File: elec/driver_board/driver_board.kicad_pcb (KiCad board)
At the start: 2 copper layers, 200 x 108 mm, 195 parts, among them IC1 MC74HC595ADR2G-Q, IC10 MC74HC595ADR2G-Q, IC11 TPL7407LADR, IC12 TPL7407LADR, IC13 MC74HC595ADR2G-Q, IC14 TPL7407LADR, IC15 TPL7407LADR, IC16 MC74HC595ADR2G-Q, IC17 TPL7407LADR, IC18 TPL7407LADR, IC19 MC74HC595ADR2G-Q, IC2 TPL7407LADR, IC20 TPL7407LADR, IC21 TPL7407LADR, IC22 MC74HC595ADR2G-Q, IC23 TPL7407LADR, IC24 TPL7407LADR, IC25 MC74HC595ADR2G-Q, IC26 TPL7407LADR, IC27 TPL7407LADR, IC28 MC74HC595ADR2G-Q, IC29 TPL7407LADR, IC3 TPL7407LADR, IC30 TPL7407LADR, IC31 MC74HC595ADR2G-Q, IC32 TPL7407LADR, IC33 TPL7407LADR, IC34 MC74HC595ADR2G-Q, IC35 TPL7407LADR, IC36 TPL7407LADR, IC37 MC74HC595ADR2G-Q, IC38 TPL7407LADR, IC39 TPL7407LADR, IC4 MC74HC595ADR2G-Q, IC40 MC74HC595ADR2G-Q, IC41 TPL7407LADR, IC42 TPL7407LADR, IC43 MC74HC595ADR2G-Q, IC44 TPL7407LADR, IC45 TPL7407LADR, IC46 MC74HC595ADR2G-Q, IC47 TPL7407LADR, IC48 TPL7407LADR, IC49 MC74HC595ADR2G-Q, IC5 TPL7407LADR, IC50 TPL7407LADR, IC51 TPL7407LADR, IC52 MC74HC595ADR2G-Q, IC53 TPL7407LADR, IC54 TPL7407LADR, IC55 MC74HC595ADR2G-Q, IC56 TPL7407LADR, IC57 TPL7407LADR, IC58 MC74HC595ADR2G-Q, IC59 TPL7407LADR, IC6 TPL7407LADR, IC60 TPL7407LADR, IC61 MC74HC595ADR2G-Q, IC62 TPL7407LADR, IC63 TPL7407LADR, IC64 MC74HC595ADR2G-Q, IC65 TPL7407LADR, IC66 TPL7407LADR, IC67 MC74HC595ADR2G-Q, IC68 TPL7407LADR, IC69 TPL7407LADR, IC7 MC74HC595ADR2G-Q, IC70 MC74HC595ADR2G-Q, IC71 TPL7407LADR, IC72 TPL7407LADR, IC8 TPL7407LADR, IC9 TPL7407LADR, J1 MOTOR_1, J10 MOTOR_0, J11 MOTOR_1, J12 MOTOR_0, J13 MOTOR_1, J14 MOTOR_0, J15 MOTOR_1, J16 MOTOR_0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

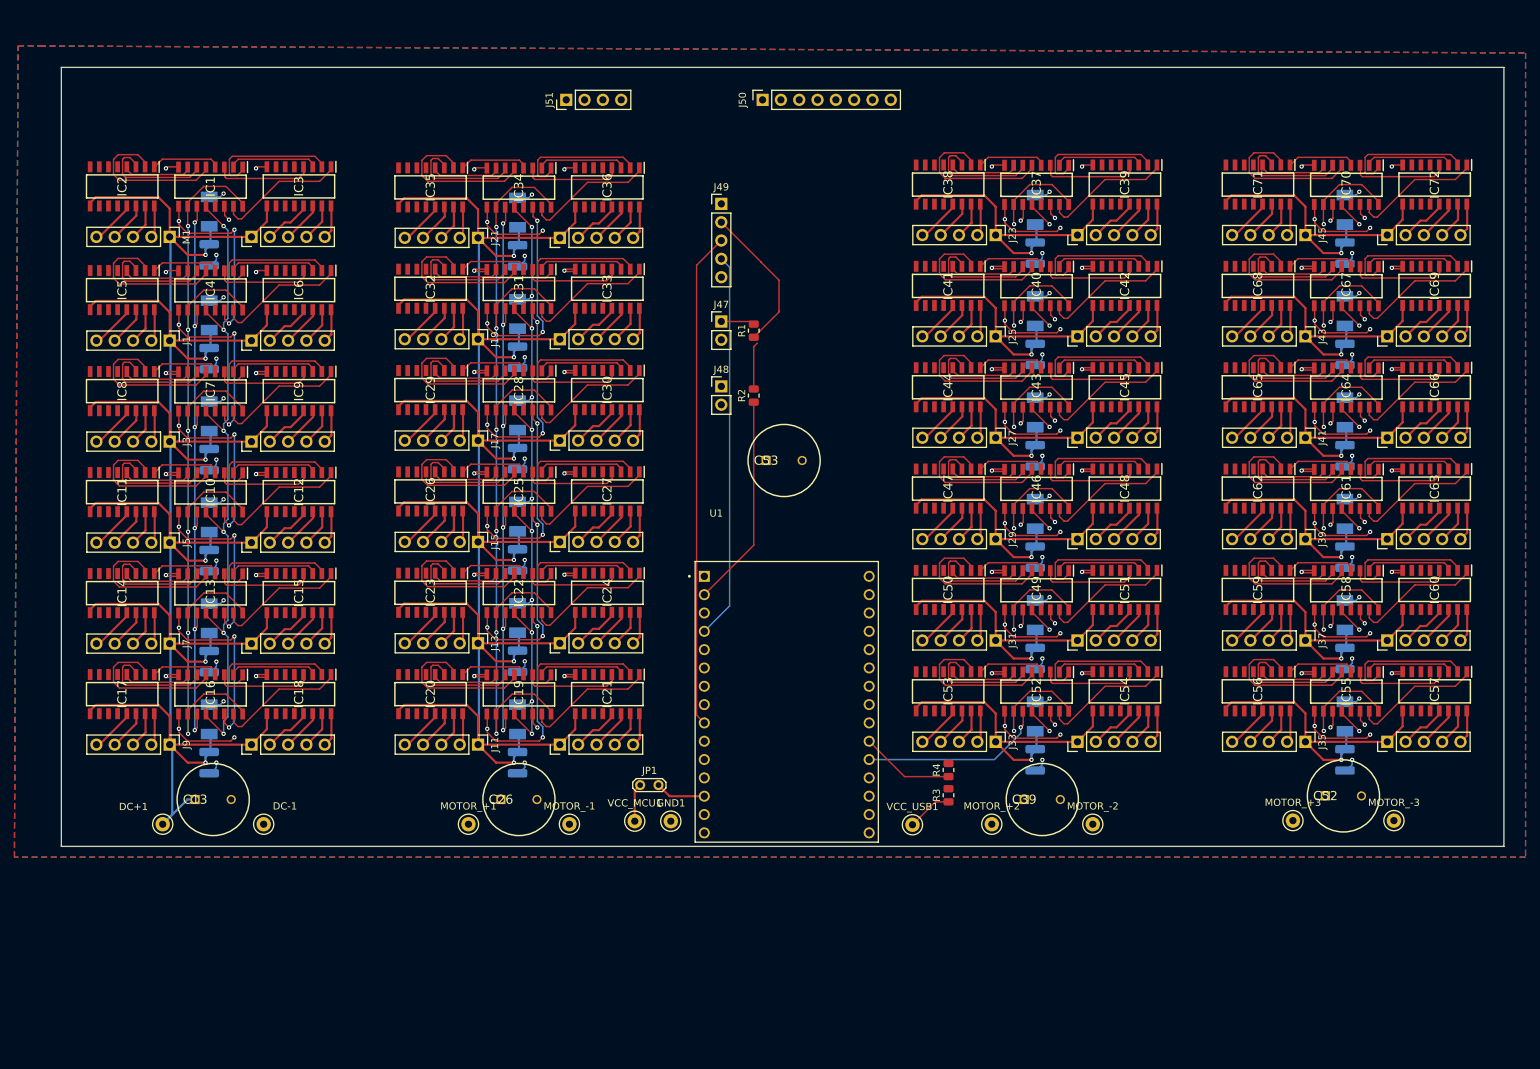
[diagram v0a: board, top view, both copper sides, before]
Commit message: [elec] New design with BKA30D-R5
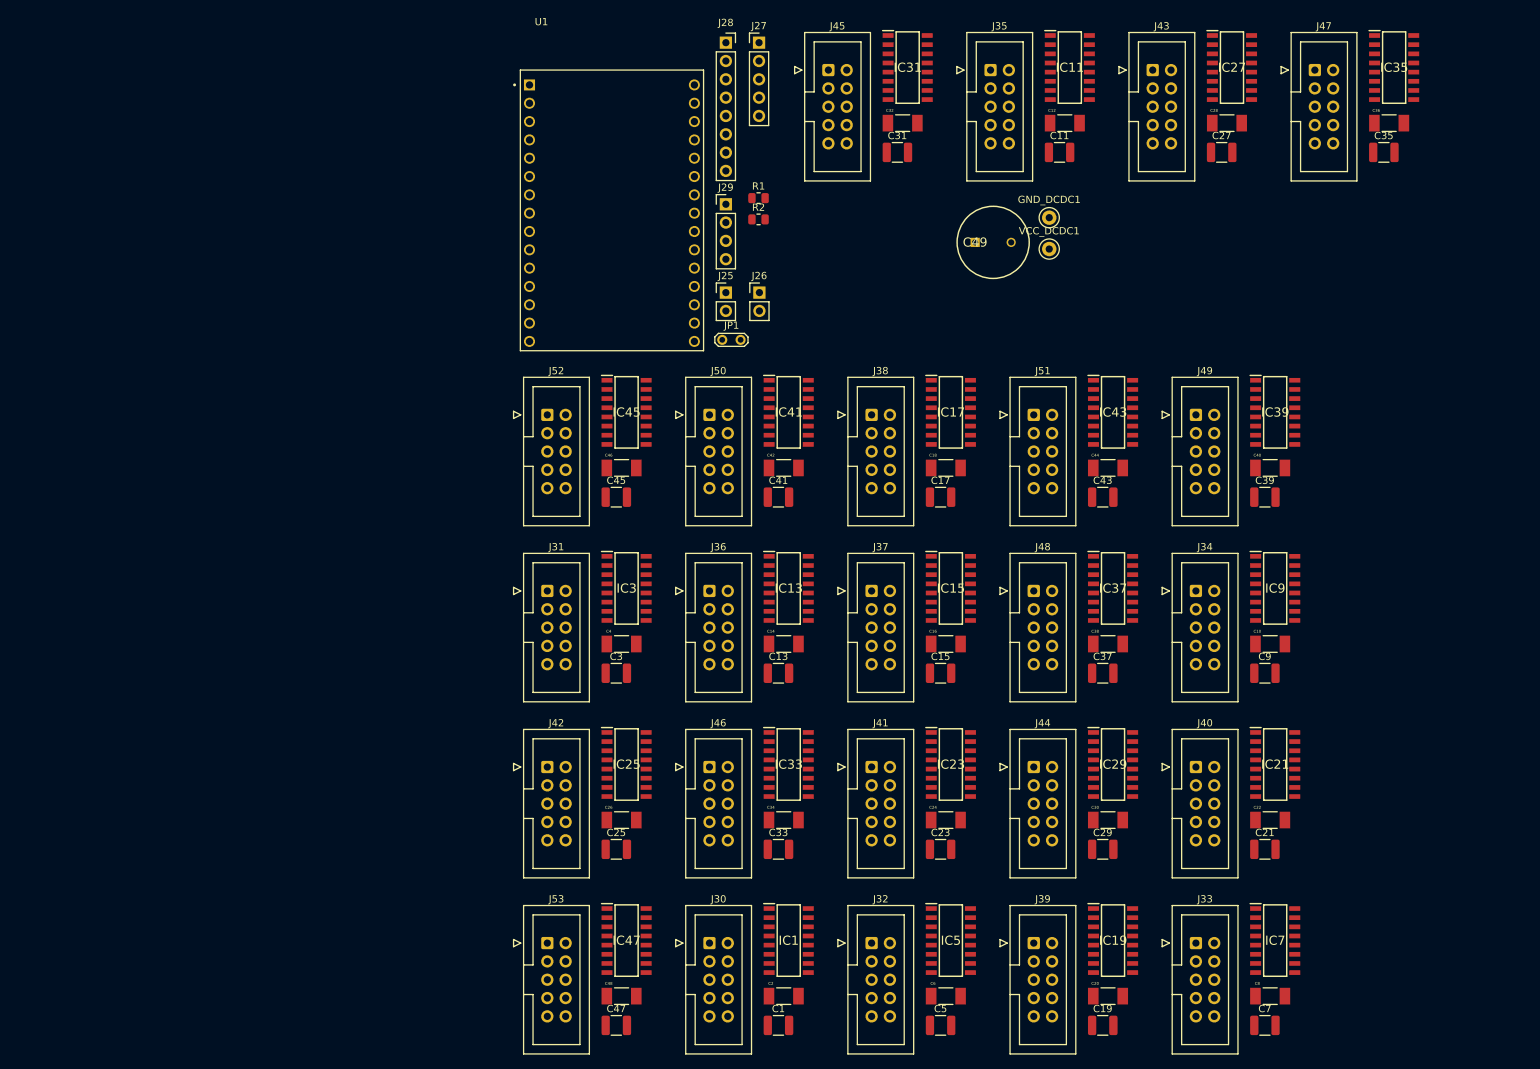
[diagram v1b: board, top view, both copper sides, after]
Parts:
- removed C50: 10µF, Capacitor_SMD:C_1210_3225Metric
- removed C51: 0.1µF, Snapeda:1808J1000392KCT_CAPC4520X200N
- removed C52, C53: ECA-1HM471, Samacsys:CAPPRD500W65D1000H2200
- removed DC+1, MOTOR_+1, MOTOR_+2, MOTOR_+3, VCC_MCU1, VCC_USB1: M+, TestPoint:TestPoint_Keystone_5000-5004_Miniature
- removed DC-1, GND1, MOTOR_-1, MOTOR_-2, MOTOR_-3: M-, TestPoint:TestPoint_Keystone_5000-5004_Miniature
- removed IC10, IC16, IC22, IC28, IC34, IC4, IC40, IC46, IC49, IC52, IC55, IC58, IC61, IC64, IC67, IC70: MC74HC595ADR2G-Q, Samacsys:SOIC127P600X175-16N
- removed IC12, IC14, IC18, IC2, IC20, IC24, IC26, IC30, IC32, IC36, IC38, IC42, IC44, IC48, IC50, IC51, IC53, IC54, IC56, IC57, IC59, IC6, IC60, IC62, IC63, IC65, IC66, IC68, IC69, IC71, IC72, IC8: TPL7407LADR, Samacsys:SOIC127P600X175-16N
- removed J1, J11, J13, J15, J17, J19, J21, J23, J3, J5, J7, J9, M1: MOTOR_1, Connector_PinHeader_2.54mm:PinHeader_1x05_P2.54mm_Vertical
- removed J10, J12, J14, J16, J18, J2, J20, J22, J24, J4, J6, J8, M2: MOTOR_0, Connector_PinHeader_2.54mm:PinHeader_1x05_P2.54mm_Vertical
- removed R3, R4: R, Resistor_SMD:R_0805_2012Metric
- added GND_DCDC1: M-, TestPoint:TestPoint_Keystone_5000-5004_Miniature, F.Cu at (166.5, 48.3)
- added J52: Conn_02x05_Counter_Clockwise, Connector_IDC:IDC-Header_2x05_P2.54mm_Vertical, F.Cu at (96.9, 75.7)
- added J53: Conn_02x05_Counter_Clockwise, Connector_IDC:IDC-Header_2x05_P2.54mm_Vertical, F.Cu at (96.9, 148.9)
- added VCC_DCDC1: M+, TestPoint:TestPoint_Keystone_5000-5004_Miniature, F.Cu at (166.5, 52.7)
- C1, C10, C11, C12, C2, C27, C28, C29, C3, C30, C31, C32, C33, C34, C35, C36, C37, C38, C4, C5, C6, C7, C8, C9: moved to F.Cu
- C13, C39: value ECA-1HM471 -> 10µF; footprint Samacsys:CAPPRD500W65D1000H2200 -> Capacitor_SMD:C_1210_3225Metric
- C14, C16, C18, C20, C22, C24, C40, C42, C44, C46, C48: value 10µF -> 0.1µF; footprint Capacitor_SMD:C_1210_3225Metric -> Snapeda:1808J1000392KCT_CAPC4520X200N; moved to F.Cu
- C15, C17, C19, C21, C23, C25, C41, C43, C45, C47: value 0.1µF -> 10µF; footprint Snapeda:1808J1000392KCT_CAPC4520X200N -> Capacitor_SMD:C_1210_3225Metric; moved to F.Cu
- C26: value ECA-1HM471 -> 0.1µF; footprint Samacsys:CAPPRD500W65D1000H2200 -> Snapeda:1808J1000392KCT_CAPC4520X200N
- C49: value 0.1µF -> ECA-1HM471; footprint Snapeda:1808J1000392KCT_CAPC4520X200N -> Samacsys:CAPPRD500W65D1000H2200; moved to F.Cu
- IC1, IC13, IC19, IC25, IC31, IC37, IC43, IC7: value MC74HC595ADR2G-Q -> TPIC6C595DG4
- IC11, IC15, IC17, IC21, IC23, IC27, IC29, IC3, IC33, IC35, IC39, IC41, IC45, IC47, IC5, IC9: value TPL7407LADR -> TPIC6C595DG4
- J25: value MOTOR_1 -> button_shutdown; footprint Connector_PinHeader_2.54mm:PinHeader_1x05_P2.54mm_Vertical -> Connector_PinHeader_2.54mm:PinHeader_1x02_P2.54mm_Vertical
- J26: value MOTOR_0 -> button_mode; footprint Connector_PinHeader_2.54mm:PinHeader_1x05_P2.54mm_Vertical -> Connector_PinHeader_2.54mm:PinHeader_1x02_P2.54mm_Vertical
- J27: value MOTOR_1 -> rotary_encoder
- J28: value MOTOR_0 -> DCF77 board; footprint Connector_PinHeader_2.54mm:PinHeader_1x05_P2.54mm_Vertical -> Connector_PinSocket_2.54mm:PinSocket_1x08_P2.54mm_Vertical
- J29: value MOTOR_1 -> RTC; footprint Connector_PinHeader_2.54mm:PinHeader_1x05_P2.54mm_Vertical -> Connector_PinHeader_2.54mm:PinHeader_1x04_P2.54mm_Vertical
- J30, J32, J34, J36, J38, J40, J42, J44, J46: value MOTOR_0 -> Conn_02x05_Counter_Clockwise; footprint Connector_PinHeader_2.54mm:PinHeader_1x05_P2.54mm_Vertical -> Connector_IDC:IDC-Header_2x05_P2.54mm_Vertical
- J31, J33, J35, J37, J39, J41, J43, J45: value MOTOR_1 -> Conn_02x05_Counter_Clockwise; footprint Connector_PinHeader_2.54mm:PinHeader_1x05_P2.54mm_Vertical -> Connector_IDC:IDC-Header_2x05_P2.54mm_Vertical
- J47: value button_shutdown -> Conn_02x05_Counter_Clockwise; footprint Connector_PinHeader_2.54mm:PinHeader_1x02_P2.54mm_Vertical -> Connector_IDC:IDC-Header_2x05_P2.54mm_Vertical
- J48: value button_mode -> Conn_02x05_Counter_Clockwise; footprint Connector_PinHeader_2.54mm:PinHeader_1x02_P2.54mm_Vertical -> Connector_IDC:IDC-Header_2x05_P2.54mm_Vertical
- J49: value rotary_encoder -> Conn_02x05_Counter_Clockwise; footprint Connector_PinHeader_2.54mm:PinHeader_1x05_P2.54mm_Vertical -> Connector_IDC:IDC-Header_2x05_P2.54mm_Vertical
- J50: value DCF77 board -> Conn_02x05_Counter_Clockwise; footprint Connector_PinSocket_2.54mm:PinSocket_1x08_P2.54mm_Vertical -> Connector_IDC:IDC-Header_2x05_P2.54mm_Vertical
- J51: value RTC -> Conn_02x05_Counter_Clockwise; footprint Connector_PinHeader_2.54mm:PinHeader_1x04_P2.54mm_Vertical -> Connector_IDC:IDC-Header_2x05_P2.54mm_Vertical
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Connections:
- C1 pad 1: /motor_driver0/VCC_MOTOR -> VCC
- C10 pad 1: /motor_driver0/VCC_MOTOR -> VCC
- C11 pad 1: /motor_driver0/VCC_MOTOR -> VCC
- C12 pad 1: /motor_driver0/VCC_MOTOR -> VCC
- C13 pad 1: /motor_driver0/VCC_MOTOR -> VCC
- C14 pad 1: /motor_driver10/VCC_MOTOR -> VCC
- C15 pad 1: /motor_driver10/VCC_MOTOR -> VCC
- C16 pad 1: /motor_driver10/VCC_MOTOR -> VCC
- C17 pad 1: /motor_driver10/VCC_MOTOR -> VCC
- C18 pad 1: /motor_driver10/VCC_MOTOR -> VCC
- C19 pad 1: /motor_driver10/VCC_MOTOR -> VCC
- C2 pad 1: /motor_driver0/VCC_MOTOR -> VCC
- C20 pad 1: /motor_driver10/VCC_MOTOR -> VCC
- C21 pad 1: /motor_driver10/VCC_MOTOR -> VCC
- C22 pad 1: /motor_driver10/VCC_MOTOR -> VCC
- C23 pad 1: /motor_driver10/VCC_MOTOR -> VCC
- C24 pad 1: /motor_driver10/VCC_MOTOR -> VCC
- C25 pad 1: /motor_driver10/VCC_MOTOR -> VCC
- C26 pad 1: /motor_driver10/VCC_MOTOR -> VCC
- C27 pad 1: /motor_driver12/VCC_MOTOR -> VCC
- C28 pad 1: /motor_driver12/VCC_MOTOR -> VCC
- C29 pad 1: /motor_driver12/VCC_MOTOR -> VCC
- C3 pad 1: /motor_driver0/VCC_MOTOR -> VCC
- C30 pad 1: /motor_driver12/VCC_MOTOR -> VCC
- C31 pad 1: /motor_driver12/VCC_MOTOR -> VCC
- C32 pad 1: /motor_driver12/VCC_MOTOR -> VCC
- C33 pad 1: /motor_driver12/VCC_MOTOR -> VCC
- C34 pad 1: /motor_driver12/VCC_MOTOR -> VCC
- C35 pad 1: /motor_driver12/VCC_MOTOR -> VCC
- C36 pad 1: /motor_driver12/VCC_MOTOR -> VCC
- C37 pad 1: /motor_driver12/VCC_MOTOR -> VCC
- C38 pad 1: /motor_driver12/VCC_MOTOR -> VCC
- C39 pad 1: /motor_driver12/VCC_MOTOR -> VCC
- C4 pad 1: /motor_driver0/VCC_MOTOR -> VCC
- C40 pad 1: /motor_driver18/VCC_MOTOR -> VCC
- C41 pad 1: /motor_driver18/VCC_MOTOR -> VCC
- C42 pad 1: /motor_driver18/VCC_MOTOR -> VCC
- C43 pad 1: /motor_driver18/VCC_MOTOR -> VCC
- C44 pad 1: /motor_driver18/VCC_MOTOR -> VCC
- C45 pad 1: /motor_driver18/VCC_MOTOR -> VCC
- C46 pad 1: /motor_driver18/VCC_MOTOR -> VCC
- C47 pad 1: /motor_driver18/VCC_MOTOR -> VCC
- C48 pad 1: /motor_driver18/VCC_MOTOR -> VCC
- C49 pad 1: /motor_driver18/VCC_MOTOR -> VCC
- C5 pad 1: /motor_driver0/VCC_MOTOR -> VCC
- C6 pad 1: /motor_driver0/VCC_MOTOR -> VCC
- C7 pad 1: /motor_driver0/VCC_MOTOR -> VCC
- C8 pad 1: /motor_driver0/VCC_MOTOR -> VCC
- C9 pad 1: /motor_driver0/VCC_MOTOR -> VCC
- IC1 pad 1: Net-(IC1-QB) -> VCC
- IC1 pad 10: VCC_CMD -> SHIFT_CLOCK
- IC1 pad 11: SHIFT_CLOCK -> /motor_driver0/M1_23
- IC1 pad 12: LATCH_CLOCK -> /motor_driver0/M1_4
- IC1 pad 13: GND -> /motor_driver0/VCC_HALL
- IC1 pad 14: /control_board/DATA_OUT -> unconnected-(IC1-DRAIN7-Pad14)
- IC1 pad 15: Net-(IC1-QA) -> LATCH_CLOCK
- IC1 pad 16: VCC_CMD -> GND
- IC1 pad 2: Net-(IC1-QC) -> /control_board/DATA_OUT
- IC1 pad 3: Net-(IC1-QD) -> /motor_driver0/M0_1
- IC1 pad 4: Net-(IC1-QE) -> /motor_driver0/M0_23
- IC1 pad 5: Net-(IC1-QF) -> /motor_driver0/M0_4
- IC1 pad 6: Net-(IC1-QG) -> /motor_driver0/M1_1
- IC1 pad 7: Net-(IC1-QH) -> VCC
- IC11 pad 1: Net-(IC10-QE) -> VCC
- IC11 pad 10: unconnected-(IC11-OUT7-Pad10) -> SHIFT_CLOCK
- IC11 pad 11: unconnected-(IC11-OUT6-Pad11) -> /motor_driver5/M1_23
- IC11 pad 12: unconnected-(IC11-OUT5-Pad12) -> /motor_driver5/M1_4
- IC11 pad 13: Net-(IC11-OUT4) -> /motor_driver5/VCC_HALL
- IC11 pad 14: Net-(IC11-OUT3) -> unconnected-(IC11-DRAIN7-Pad14)
- IC11 pad 15: Net-(IC11-OUT2) -> LATCH_CLOCK
- IC11 pad 16: Net-(IC11-OUT1) -> GND
- IC11 pad 2: Net-(IC10-QF) -> /motor_driver4/DATA_OUT
- IC11 pad 3: Net-(IC10-QG) -> /motor_driver5/M0_1
- IC11 pad 4: Net-(IC10-QH) -> /motor_driver5/M0_23
- IC11 pad 5: unconnected-(IC11-IN5-Pad5) -> /motor_driver5/M0_4
- IC11 pad 6: unconnected-(IC11-IN6-Pad6) -> /motor_driver5/M1_1
- IC11 pad 7: unconnected-(IC11-IN7-Pad7) -> VCC
- IC11 pad 9: /motor_driver0/VCC_MOTOR -> /motor_driver5/DATA_OUT
- IC13 pad 1: Net-(IC13-QB) -> VCC
- IC13 pad 10: VCC_CMD -> SHIFT_CLOCK
- IC13 pad 11: SHIFT_CLOCK -> /motor_driver6/M1_23
- IC13 pad 12: LATCH_CLOCK -> /motor_driver6/M1_4
- IC13 pad 13: GND -> /motor_driver6/VCC_HALL
- IC13 pad 14: /motor_driver3/DATA_OUT -> unconnected-(IC13-DRAIN7-Pad14)
- IC13 pad 15: Net-(IC13-QA) -> LATCH_CLOCK
- IC13 pad 16: VCC_CMD -> GND
- IC13 pad 2: Net-(IC13-QC) -> /motor_driver5/DATA_OUT
- IC13 pad 3: Net-(IC13-QD) -> /motor_driver6/M0_1
- IC13 pad 4: Net-(IC13-QE) -> /motor_driver6/M0_23
- IC13 pad 5: Net-(IC13-QF) -> /motor_driver6/M0_4
- IC13 pad 6: Net-(IC13-QG) -> /motor_driver6/M1_1
- IC13 pad 7: Net-(IC13-QH) -> VCC
- IC13 pad 9: /motor_driver4/DATA_OUT -> /motor_driver6/DATA_OUT
- IC15 pad 1: Net-(IC13-QA) -> VCC
- IC15 pad 10: unconnected-(IC15-OUT7-Pad10) -> SHIFT_CLOCK
- IC15 pad 11: unconnected-(IC15-OUT6-Pad11) -> /motor_driver7/M1_23
- IC15 pad 12: unconnected-(IC15-OUT5-Pad12) -> /motor_driver7/M1_4
- IC15 pad 13: Net-(IC15-OUT4) -> /motor_driver7/VCC_HALL
- IC15 pad 14: Net-(IC15-OUT3) -> unconnected-(IC15-DRAIN7-Pad14)
- IC15 pad 15: Net-(IC15-OUT2) -> LATCH_CLOCK
- IC15 pad 16: Net-(IC15-OUT1) -> GND
- IC15 pad 2: Net-(IC13-QB) -> /motor_driver6/DATA_OUT
- IC15 pad 3: Net-(IC13-QC) -> /motor_driver7/M0_1
- IC15 pad 4: Net-(IC13-QD) -> /motor_driver7/M0_23
- IC15 pad 5: unconnected-(IC15-IN5-Pad5) -> /motor_driver7/M0_4
- IC15 pad 6: unconnected-(IC15-IN6-Pad6) -> /motor_driver7/M1_1
- IC15 pad 7: unconnected-(IC15-IN7-Pad7) -> VCC
- IC15 pad 9: /motor_driver0/VCC_MOTOR -> /motor_driver7/DATA_OUT
- IC17 pad 1: Net-(IC16-QE) -> VCC
- IC17 pad 10: unconnected-(IC17-OUT7-Pad10) -> SHIFT_CLOCK
- IC17 pad 11: unconnected-(IC17-OUT6-Pad11) -> /motor_driver8/M1_23
- IC17 pad 12: unconnected-(IC17-OUT5-Pad12) -> /motor_driver8/M1_4
- IC17 pad 13: Net-(IC17-OUT4) -> /motor_driver8/VCC_HALL
- IC17 pad 14: Net-(IC17-OUT3) -> unconnected-(IC17-DRAIN7-Pad14)
- IC17 pad 15: Net-(IC17-OUT2) -> LATCH_CLOCK
- IC17 pad 16: Net-(IC17-OUT1) -> GND
- IC17 pad 2: Net-(IC16-QF) -> /motor_driver7/DATA_OUT
- IC17 pad 3: Net-(IC16-QG) -> /motor_driver8/M0_1
- IC17 pad 4: Net-(IC16-QH) -> /motor_driver8/M0_23
- IC17 pad 5: unconnected-(IC17-IN5-Pad5) -> /motor_driver8/M0_4
- IC17 pad 6: unconnected-(IC17-IN6-Pad6) -> /motor_driver8/M1_1
- IC17 pad 7: unconnected-(IC17-IN7-Pad7) -> VCC
- IC17 pad 9: /motor_driver0/VCC_MOTOR -> /motor_driver8/DATA_OUT
- IC19 pad 1: Net-(IC19-QB) -> VCC
- IC19 pad 10: VCC_CMD -> SHIFT_CLOCK
- IC19 pad 11: SHIFT_CLOCK -> /motor_driver9/M1_23
- IC19 pad 12: LATCH_CLOCK -> /motor_driver9/M1_4
- IC19 pad 13: GND -> /motor_driver9/VCC_HALL
- IC19 pad 14: /motor_driver5/DATA_OUT -> unconnected-(IC19-DRAIN7-Pad14)
- IC19 pad 15: Net-(IC19-QA) -> LATCH_CLOCK
- IC19 pad 16: VCC_CMD -> GND
- IC19 pad 2: Net-(IC19-QC) -> /motor_driver8/DATA_OUT
- IC19 pad 3: Net-(IC19-QD) -> /motor_driver9/M0_1
- IC19 pad 4: Net-(IC19-QE) -> /motor_driver9/M0_23
- IC19 pad 5: Net-(IC19-QF) -> /motor_driver9/M0_4
- IC19 pad 6: Net-(IC19-QG) -> /motor_driver9/M1_1
- IC19 pad 7: Net-(IC19-QH) -> VCC
- IC19 pad 9: /motor_driver6/DATA_OUT -> /motor_driver10/DATA_IN
- IC21 pad 1: Net-(IC19-QA) -> VCC
- IC21 pad 10: unconnected-(IC21-OUT7-Pad10) -> SHIFT_CLOCK
- IC21 pad 11: unconnected-(IC21-OUT6-Pad11) -> /motor_driver10/M1_23
- IC21 pad 12: unconnected-(IC21-OUT5-Pad12) -> /motor_driver10/M1_4
- IC21 pad 13: Net-(IC21-OUT4) -> /motor_driver10/VCC_HALL
- IC21 pad 14: Net-(IC21-OUT3) -> unconnected-(IC21-DRAIN7-Pad14)
- IC21 pad 15: Net-(IC21-OUT2) -> LATCH_CLOCK
- IC21 pad 16: Net-(IC21-OUT1) -> GND
- IC21 pad 2: Net-(IC19-QB) -> /motor_driver10/DATA_IN
- IC21 pad 3: Net-(IC19-QC) -> /motor_driver10/M0_1
- IC21 pad 4: Net-(IC19-QD) -> /motor_driver10/M0_23
- IC21 pad 5: unconnected-(IC21-IN5-Pad5) -> /motor_driver10/M0_4
- IC21 pad 6: unconnected-(IC21-IN6-Pad6) -> /motor_driver10/M1_1
- IC21 pad 7: unconnected-(IC21-IN7-Pad7) -> VCC
- IC21 pad 9: /motor_driver10/VCC_MOTOR -> /motor_driver10/DATA_OUT
- IC23 pad 1: Net-(IC22-QE) -> VCC
- IC23 pad 10: unconnected-(IC23-OUT7-Pad10) -> SHIFT_CLOCK
- IC23 pad 11: unconnected-(IC23-OUT6-Pad11) -> /motor_driver11/M1_23
- IC23 pad 12: unconnected-(IC23-OUT5-Pad12) -> /motor_driver11/M1_4
- IC23 pad 13: Net-(IC23-OUT4) -> /motor_driver11/VCC_HALL
- IC23 pad 14: Net-(IC23-OUT3) -> unconnected-(IC23-DRAIN7-Pad14)
- IC23 pad 15: Net-(IC23-OUT2) -> LATCH_CLOCK
- IC23 pad 16: Net-(IC23-OUT1) -> GND
- IC23 pad 2: Net-(IC22-QF) -> /motor_driver10/DATA_OUT
- IC23 pad 3: Net-(IC22-QG) -> /motor_driver11/M0_1
- IC23 pad 4: Net-(IC22-QH) -> /motor_driver11/M0_23
- IC23 pad 5: unconnected-(IC23-IN5-Pad5) -> /motor_driver11/M0_4
- IC23 pad 6: unconnected-(IC23-IN6-Pad6) -> /motor_driver11/M1_1
- IC23 pad 7: unconnected-(IC23-IN7-Pad7) -> VCC
- IC23 pad 9: /motor_driver10/VCC_MOTOR -> /motor_driver11/DATA_OUT
- IC25 pad 1: Net-(IC25-QB) -> VCC
- IC25 pad 10: VCC_CMD -> SHIFT_CLOCK
- IC25 pad 11: SHIFT_CLOCK -> /motor_driver12/M1_23
- IC25 pad 12: LATCH_CLOCK -> /motor_driver12/M1_4
- IC25 pad 13: GND -> /motor_driver12/VCC_HALL
- IC25 pad 14: /motor_driver7/DATA_OUT -> unconnected-(IC25-DRAIN7-Pad14)
- IC25 pad 15: Net-(IC25-QA) -> LATCH_CLOCK
- IC25 pad 16: VCC_CMD -> GND
- IC25 pad 2: Net-(IC25-QC) -> /motor_driver11/DATA_OUT
- IC25 pad 3: Net-(IC25-QD) -> /motor_driver12/M0_1
- IC25 pad 4: Net-(IC25-QE) -> /motor_driver12/M0_23
- IC25 pad 5: Net-(IC25-QF) -> /motor_driver12/M0_4
- IC25 pad 6: Net-(IC25-QG) -> /motor_driver12/M1_1
- IC25 pad 7: Net-(IC25-QH) -> VCC
- IC25 pad 9: /motor_driver8/DATA_OUT -> /motor_driver12/DATA_OUT
- IC27 pad 1: Net-(IC25-QA) -> VCC
- IC27 pad 10: unconnected-(IC27-OUT7-Pad10) -> SHIFT_CLOCK
- IC27 pad 11: unconnected-(IC27-OUT6-Pad11) -> /motor_driver13/M1_23
- IC27 pad 12: unconnected-(IC27-OUT5-Pad12) -> /motor_driver13/M1_4
- IC27 pad 13: Net-(IC27-OUT4) -> /motor_driver13/VCC_HALL
- IC27 pad 14: Net-(IC27-OUT3) -> unconnected-(IC27-DRAIN7-Pad14)
- IC27 pad 15: Net-(IC27-OUT2) -> LATCH_CLOCK
- IC27 pad 16: Net-(IC27-OUT1) -> GND
- IC27 pad 2: Net-(IC25-QB) -> /motor_driver12/DATA_OUT
- IC27 pad 3: Net-(IC25-QC) -> /motor_driver13/M0_1
- IC27 pad 4: Net-(IC25-QD) -> /motor_driver13/M0_23
- IC27 pad 5: unconnected-(IC27-IN5-Pad5) -> /motor_driver13/M0_4
- IC27 pad 6: unconnected-(IC27-IN6-Pad6) -> /motor_driver13/M1_1
- IC27 pad 7: unconnected-(IC27-IN7-Pad7) -> VCC
- IC27 pad 9: /motor_driver10/VCC_MOTOR -> /motor_driver13/DATA_OUT
- IC29 pad 1: Net-(IC28-QE) -> VCC
- IC29 pad 10: unconnected-(IC29-OUT7-Pad10) -> SHIFT_CLOCK
- IC29 pad 11: unconnected-(IC29-OUT6-Pad11) -> /motor_driver14/M1_23
- IC29 pad 12: unconnected-(IC29-OUT5-Pad12) -> /motor_driver14/M1_4
- IC29 pad 13: Net-(IC29-OUT4) -> /motor_driver14/VCC_HALL
- IC29 pad 14: Net-(IC29-OUT3) -> unconnected-(IC29-DRAIN7-Pad14)
- IC29 pad 15: Net-(IC29-OUT2) -> LATCH_CLOCK
- IC29 pad 16: Net-(IC29-OUT1) -> GND
- IC29 pad 2: Net-(IC28-QF) -> /motor_driver13/DATA_OUT
- IC29 pad 3: Net-(IC28-QG) -> /motor_driver14/M0_1
- IC29 pad 4: Net-(IC28-QH) -> /motor_driver14/M0_23
- IC29 pad 5: unconnected-(IC29-IN5-Pad5) -> /motor_driver14/M0_4
- IC29 pad 6: unconnected-(IC29-IN6-Pad6) -> /motor_driver14/M1_1
- IC29 pad 7: unconnected-(IC29-IN7-Pad7) -> VCC
- IC29 pad 9: /motor_driver10/VCC_MOTOR -> /motor_driver14/DATA_OUT
- IC3 pad 1: Net-(IC1-QA) -> VCC
- IC3 pad 10: unconnected-(IC3-OUT7-Pad10) -> SHIFT_CLOCK
- IC3 pad 11: unconnected-(IC3-OUT6-Pad11) -> /motor_driver1/M1_23
- IC3 pad 12: unconnected-(IC3-OUT5-Pad12) -> /motor_driver1/M1_4
- IC3 pad 13: Net-(IC3-OUT4) -> /motor_driver1/VCC_HALL
- IC3 pad 14: Net-(IC3-OUT3) -> unconnected-(IC3-DRAIN7-Pad14)
- IC3 pad 15: Net-(IC3-OUT2) -> LATCH_CLOCK
- IC3 pad 16: Net-(IC3-OUT1) -> GND
- IC3 pad 2: Net-(IC1-QB) -> /motor_driver0/DATA_OUT
- IC3 pad 3: Net-(IC1-QC) -> /motor_driver1/M0_1
- IC3 pad 4: Net-(IC1-QD) -> /motor_driver1/M0_23
- IC3 pad 5: unconnected-(IC3-IN5-Pad5) -> /motor_driver1/M0_4
- IC3 pad 6: unconnected-(IC3-IN6-Pad6) -> /motor_driver1/M1_1
- IC3 pad 7: unconnected-(IC3-IN7-Pad7) -> VCC
- IC3 pad 9: /motor_driver0/VCC_MOTOR -> /motor_driver1/DATA_OUT
- IC31 pad 1: Net-(IC31-QB) -> VCC
- IC31 pad 10: VCC_CMD -> SHIFT_CLOCK
- IC31 pad 11: SHIFT_CLOCK -> /motor_driver15/M1_23
- IC31 pad 12: LATCH_CLOCK -> /motor_driver15/M1_4
- IC31 pad 13: GND -> /motor_driver15/VCC_HALL
- IC31 pad 14: /motor_driver10/DATA_IN -> unconnected-(IC31-DRAIN7-Pad14)
- IC31 pad 15: Net-(IC31-QA) -> LATCH_CLOCK
- IC31 pad 16: VCC_CMD -> GND
- IC31 pad 2: Net-(IC31-QC) -> /motor_driver14/DATA_OUT
- IC31 pad 3: Net-(IC31-QD) -> /motor_driver15/M0_1
- IC31 pad 4: Net-(IC31-QE) -> /motor_driver15/M0_23
- IC31 pad 5: Net-(IC31-QF) -> /motor_driver15/M0_4
- IC31 pad 6: Net-(IC31-QG) -> /motor_driver15/M1_1
- IC31 pad 7: Net-(IC31-QH) -> VCC
- IC31 pad 9: /motor_driver10/DATA_OUT -> /motor_driver15/DATA_OUT
- IC33 pad 1: Net-(IC31-QA) -> VCC
- IC33 pad 10: unconnected-(IC33-OUT7-Pad10) -> SHIFT_CLOCK
- IC33 pad 11: unconnected-(IC33-OUT6-Pad11) -> /motor_driver16/M1_23
- IC33 pad 12: unconnected-(IC33-OUT5-Pad12) -> /motor_driver16/M1_4
- IC33 pad 13: Net-(IC33-OUT4) -> /motor_driver16/VCC_HALL
- IC33 pad 14: Net-(IC33-OUT3) -> unconnected-(IC33-DRAIN7-Pad14)
- IC33 pad 15: Net-(IC33-OUT2) -> LATCH_CLOCK
- IC33 pad 16: Net-(IC33-OUT1) -> GND
- IC33 pad 2: Net-(IC31-QB) -> /motor_driver15/DATA_OUT
- IC33 pad 3: Net-(IC31-QC) -> /motor_driver16/M0_1
- IC33 pad 4: Net-(IC31-QD) -> /motor_driver16/M0_23
- IC33 pad 5: unconnected-(IC33-IN5-Pad5) -> /motor_driver16/M0_4
- IC33 pad 6: unconnected-(IC33-IN6-Pad6) -> /motor_driver16/M1_1
- IC33 pad 7: unconnected-(IC33-IN7-Pad7) -> VCC
- IC33 pad 9: /motor_driver10/VCC_MOTOR -> /motor_driver16/DATA_OUT
- IC35 pad 1: Net-(IC34-QE) -> VCC
- IC35 pad 10: unconnected-(IC35-OUT7-Pad10) -> SHIFT_CLOCK
- IC35 pad 11: unconnected-(IC35-OUT6-Pad11) -> /motor_driver17/M1_23
- IC35 pad 12: unconnected-(IC35-OUT5-Pad12) -> /motor_driver17/M1_4
- IC35 pad 13: Net-(IC35-OUT4) -> /motor_driver17/VCC_HALL
- IC35 pad 14: Net-(IC35-OUT3) -> unconnected-(IC35-DRAIN7-Pad14)
- IC35 pad 15: Net-(IC35-OUT2) -> LATCH_CLOCK
- IC35 pad 16: Net-(IC35-OUT1) -> GND
- IC35 pad 2: Net-(IC34-QF) -> /motor_driver16/DATA_OUT
- IC35 pad 3: Net-(IC34-QG) -> /motor_driver17/M0_1
- IC35 pad 4: Net-(IC34-QH) -> /motor_driver17/M0_23
- IC35 pad 5: unconnected-(IC35-IN5-Pad5) -> /motor_driver17/M0_4
- IC35 pad 6: unconnected-(IC35-IN6-Pad6) -> /motor_driver17/M1_1
- IC35 pad 7: unconnected-(IC35-IN7-Pad7) -> VCC
- IC35 pad 9: /motor_driver10/VCC_MOTOR -> /motor_driver17/DATA_OUT
- IC37 pad 1: Net-(IC37-QB) -> VCC
- IC37 pad 10: VCC_CMD -> SHIFT_CLOCK
- IC37 pad 11: SHIFT_CLOCK -> /motor_driver18/M1_23
- IC37 pad 12: LATCH_CLOCK -> /motor_driver18/M1_4
- IC37 pad 13: GND -> /motor_driver18/VCC_HALL
- IC37 pad 14: /motor_driver11/DATA_OUT -> unconnected-(IC37-DRAIN7-Pad14)
- IC37 pad 15: Net-(IC37-QA) -> LATCH_CLOCK
- IC37 pad 16: VCC_CMD -> GND
- IC37 pad 2: Net-(IC37-QC) -> /motor_driver17/DATA_OUT
- IC37 pad 3: Net-(IC37-QD) -> /motor_driver18/M0_1
- IC37 pad 4: Net-(IC37-QE) -> /motor_driver18/M0_23
- IC37 pad 5: Net-(IC37-QF) -> /motor_driver18/M0_4
- IC37 pad 6: Net-(IC37-QG) -> /motor_driver18/M1_1
- IC37 pad 7: Net-(IC37-QH) -> VCC
- IC37 pad 9: /motor_driver12/DATA_OUT -> /motor_driver18/DATA_OUT
- IC39 pad 1: Net-(IC37-QA) -> VCC
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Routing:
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- removed copper zone on B.Cu, net GND
- removed copper zone on F.Cu, net GND
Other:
- board outline removed

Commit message: [elec] continue routing
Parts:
- removed IC25, IC27, IC29, IC31, IC33, IC35, IC37, IC39, IC41, IC43, IC45, IC47: TPIC6C595DG4, Samacsys:SOIC127P600X175-16N
- removed J30, J31, J32, J33, J34, J35, J36, J37, J38, J39, J40, J41, J42, J43, J44, J45, J46, J47, J48, J49, J50, J51, J52, J53: Conn_02x05_Counter_Clockwise, Connector_IDC:IDC-Header_2x05_P2.54mm_Vertical
- added Cl1: 4.2nF, Capacitor_SMD:C_1206_3216Metric, F.Cu at (48.1, 32.6)
- added IC10: TPIC6C595DG4, Samacsys:SOIC127P600X175-16N, F.Cu at (164.5, 54.0)
- added IC12: TPIC6C595DG4, Samacsys:SOIC127P600X175-16N, F.Cu at (164.5, 25.9)
- added IC14: TPIC6C595DG4, Samacsys:SOIC127P600X175-16N, F.Cu at (189.2, 39.9)
- added IC16: TPIC6C595DG4, Samacsys:SOIC127P600X175-16N, F.Cu at (213.9, 54.0)
- added IC18: TPIC6C595DG4, Samacsys:SOIC127P600X175-16N, F.Cu at (213.9, 25.9)
- added IC2: TPIC6C595DG4, Samacsys:SOIC127P600X175-16N, F.Cu at (90.5, 39.9)
- added IC20: TPIC6C595DG4, Samacsys:SOIC127P600X175-16N, F.Cu at (238.6, 39.9)
- added IC22: TPIC6C595DG4, Samacsys:SOIC127P600X175-16N, F.Cu at (263.3, 54.0)
- added IC24: TPIC6C595DG4, Samacsys:SOIC127P600X175-16N, F.Cu at (263.3, 25.9)
- added IC4: TPIC6C595DG4, Samacsys:SOIC127P600X175-16N, F.Cu at (115.1, 54.0)
- added IC6: TPIC6C595DG4, Samacsys:SOIC127P600X175-16N, F.Cu at (115.1, 25.9)
- added IC8: TPIC6C595DG4, Samacsys:SOIC127P600X175-16N, F.Cu at (139.8, 39.9)
- added J1: Connector to the motor board, Connector_JST:JST_PH_B10B-PH-K_1x10_P2.00mm_Vertical, F.Cu at (87.4, 18.3)
- added J10: Connector to the motor board, Connector_JST:JST_PH_B10B-PH-K_1x10_P2.00mm_Vertical, F.Cu at (161.5, 46.4)
- added J11: Connector to the motor board, Connector_JST:JST_PH_B10B-PH-K_1x10_P2.00mm_Vertical, F.Cu at (161.5, 32.3)
- added J12: Connector to the motor board, Connector_JST:JST_PH_B10B-PH-K_1x10_P2.00mm_Vertical, F.Cu at (161.5, 18.3)
- added J13: Connector to the motor board, Connector_JST:JST_PH_B10B-PH-K_1x10_P2.00mm_Vertical, F.Cu at (186.2, 18.3)
- added J14: Connector to the motor board, Connector_JST:JST_PH_B10B-PH-K_1x10_P2.00mm_Vertical, F.Cu at (186.2, 32.3)
- added J15: Connector to the motor board, Connector_JST:JST_PH_B10B-PH-K_1x10_P2.00mm_Vertical, F.Cu at (186.2, 46.4)
- added J16: Connector to the motor board, Connector_JST:JST_PH_B10B-PH-K_1x10_P2.00mm_Vertical, F.Cu at (210.9, 46.4)
- added J17: Connector to the motor board, Connector_JST:JST_PH_B10B-PH-K_1x10_P2.00mm_Vertical, F.Cu at (210.9, 32.3)
- added J18: Connector to the motor board, Connector_JST:JST_PH_B10B-PH-K_1x10_P2.00mm_Vertical, F.Cu at (210.9, 18.3)
- added J19: Connector to the motor board, Connector_JST:JST_PH_B10B-PH-K_1x10_P2.00mm_Vertical, F.Cu at (235.5, 18.3)
- added J2: Connector to the motor board, Connector_JST:JST_PH_B10B-PH-K_1x10_P2.00mm_Vertical, F.Cu at (87.4, 32.3)
- added J20: Connector to the motor board, Connector_JST:JST_PH_B10B-PH-K_1x10_P2.00mm_Vertical, F.Cu at (235.5, 32.3)
- added J21: Connector to the motor board, Connector_JST:JST_PH_B10B-PH-K_1x10_P2.00mm_Vertical, F.Cu at (235.5, 46.4)
- added J22: Connector to the motor board, Connector_JST:JST_PH_B10B-PH-K_1x10_P2.00mm_Vertical, F.Cu at (260.2, 46.4)
- added J23: Connector to the motor board, Connector_JST:JST_PH_B10B-PH-K_1x10_P2.00mm_Vertical, F.Cu at (260.2, 32.3)
- added J24: Connector to the motor board, Connector_JST:JST_PH_B10B-PH-K_1x10_P2.00mm_Vertical, F.Cu at (260.2, 18.3)
- added J3: Connector to the motor board, Connector_JST:JST_PH_B10B-PH-K_1x10_P2.00mm_Vertical, F.Cu at (87.4, 46.4)
- added J4: Connector to the motor board, Connector_JST:JST_PH_B10B-PH-K_1x10_P2.00mm_Vertical, F.Cu at (112.1, 46.4)
- added J5: Connector to the motor board, Connector_JST:JST_PH_B10B-PH-K_1x10_P2.00mm_Vertical, F.Cu at (112.1, 32.3)
- added J6: Connector to the motor board, Connector_JST:JST_PH_B10B-PH-K_1x10_P2.00mm_Vertical, F.Cu at (112.1, 18.3)
- added J7: Connector to the motor board, Connector_JST:JST_PH_B10B-PH-K_1x10_P2.00mm_Vertical, F.Cu at (136.8, 18.3)
- added J8: Connector to the motor board, Connector_JST:JST_PH_B10B-PH-K_1x10_P2.00mm_Vertical, F.Cu at (136.8, 32.3)
- added J9: Connector to the motor board, Connector_JST:JST_PH_B10B-PH-K_1x10_P2.00mm_Vertical, F.Cu at (136.8, 46.4)
- added Rl1: 4.7k, Capacitor_SMD:C_1206_3216Metric, F.Cu at (48.1, 36.0)
- C1, C11, C13, C15, C17, C19, C21, C23, C25, C27, C29, C3, C31, C33, C35, C37, C39, C41, C43, C45, C47, C5, C7, C9: value 10µF -> 47µF; footprint Capacitor_SMD:C_1210_3225Metric -> Capacitor_SMD:C_1210_3225Metric_Pad1.33x2.70mm_HandSolder
- C10, C12, C14, C16, C18, C2, C20, C22, C24, C26, C28, C30, C32, C34, C36, C38, C4, C40, C42, C44, C46, C48, C6, C8: footprint Snapeda:1808J1000392KCT_CAPC4520X200N -> Capacitor_SMD:C_1210_3225Metric_Pad1.33x2.70mm_HandSolder
- moved C47 215.8 mm to (275.0, 25.6), turned to -90 degrees
- moved C48 209.5 mm to (271.0, 25.6), turned to -90 degrees
- moved C45 175.1 mm to (275.0, 39.6), turned to -90 degrees
- moved C46 169.5 mm to (271.0, 39.6), turned to -90 degrees
- moved C25 145.2 mm to (200.9, 25.6), turned to -90 degrees
- moved C26 139.1 mm to (196.9, 25.6), turned to -90 degrees
- moved IC23 138.9 mm to (263.3, 39.9), turned to -90 degrees
- moved IC19 138.0 mm to (238.6, 25.9), turned to -90 degrees
- moved C1 137.3 mm to (102.1, 25.6), turned to -90 degrees
- moved C33 136.4 mm to (225.6, 39.6), turned to -90 degrees
- moved IC7 135.6 mm to (139.8, 25.9), turned to -90 degrees
- moved C2 134.4 mm to (98.1, 25.6), turned to -90 degrees
- moved C49 133.1 mm to (24.0, 36.0)
- moved GND_DCDC1 133.1 mm to (34.3, 32.6)
- moved VCC_DCDC1 133.1 mm to (34.3, 36.9)
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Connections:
- net /control_board/VCC_3V3 renamed VCC_3V3
- IC1 pad 10: SHIFT_CLOCK -> LATCH_CLOCK
- IC1 pad 15: LATCH_CLOCK -> SHIFT_CLOCK
- IC11 pad 10: SHIFT_CLOCK -> LATCH_CLOCK
- IC11 pad 11: /motor_driver5/M1_23 -> /motor_driver10/M1_23
- IC11 pad 12: /motor_driver5/M1_4 -> /motor_driver10/M1_4
- IC11 pad 13: /motor_driver5/VCC_HALL -> /motor_driver10/VCC_HALL
- IC11 pad 15: LATCH_CLOCK -> SHIFT_CLOCK
- IC11 pad 2: /motor_driver4/DATA_OUT -> /motor_driver10/DATA_IN
- IC11 pad 3: /motor_driver5/M0_1 -> /motor_driver10/M0_1
- IC11 pad 4: /motor_driver5/M0_23 -> /motor_driver10/M0_23
- IC11 pad 5: /motor_driver5/M0_4 -> /motor_driver10/M0_4
- IC11 pad 6: /motor_driver5/M1_1 -> /motor_driver10/M1_1
- IC11 pad 9: /motor_driver5/DATA_OUT -> /motor_driver10/DATA_OUT
- IC13 pad 10: SHIFT_CLOCK -> LATCH_CLOCK
- IC13 pad 11: /motor_driver6/M1_23 -> /motor_driver12/M1_23
- IC13 pad 12: /motor_driver6/M1_4 -> /motor_driver12/M1_4
- IC13 pad 13: /motor_driver6/VCC_HALL -> /motor_driver12/VCC_HALL
- IC13 pad 15: LATCH_CLOCK -> SHIFT_CLOCK
- IC13 pad 2: /motor_driver5/DATA_OUT -> /motor_driver11/DATA_OUT
- IC13 pad 3: /motor_driver6/M0_1 -> /motor_driver12/M0_1
- IC13 pad 4: /motor_driver6/M0_23 -> /motor_driver12/M0_23
- IC13 pad 5: /motor_driver6/M0_4 -> /motor_driver12/M0_4
- IC13 pad 6: /motor_driver6/M1_1 -> /motor_driver12/M1_1
- IC13 pad 9: /motor_driver6/DATA_OUT -> /motor_driver12/DATA_OUT
- IC15 pad 10: SHIFT_CLOCK -> LATCH_CLOCK
- IC15 pad 11: /motor_driver7/M1_23 -> /motor_driver14/M1_23
- IC15 pad 12: /motor_driver7/M1_4 -> /motor_driver14/M1_4
- IC15 pad 13: /motor_driver7/VCC_HALL -> /motor_driver14/VCC_HALL
- IC15 pad 15: LATCH_CLOCK -> SHIFT_CLOCK
- IC15 pad 2: /motor_driver6/DATA_OUT -> /motor_driver13/DATA_OUT
- IC15 pad 3: /motor_driver7/M0_1 -> /motor_driver14/M0_1
- IC15 pad 4: /motor_driver7/M0_23 -> /motor_driver14/M0_23
- IC15 pad 5: /motor_driver7/M0_4 -> /motor_driver14/M0_4
- IC15 pad 6: /motor_driver7/M1_1 -> /motor_driver14/M1_1
- IC15 pad 9: /motor_driver7/DATA_OUT -> /motor_driver14/DATA_OUT
- IC17 pad 10: SHIFT_CLOCK -> LATCH_CLOCK
- IC17 pad 11: /motor_driver8/M1_23 -> /motor_driver16/M1_23
- IC17 pad 12: /motor_driver8/M1_4 -> /motor_driver16/M1_4
- IC17 pad 13: /motor_driver8/VCC_HALL -> /motor_driver16/VCC_HALL
- IC17 pad 15: LATCH_CLOCK -> SHIFT_CLOCK
- IC17 pad 2: /motor_driver7/DATA_OUT -> /motor_driver15/DATA_OUT
- IC17 pad 3: /motor_driver8/M0_1 -> /motor_driver16/M0_1
- IC17 pad 4: /motor_driver8/M0_23 -> /motor_driver16/M0_23
- IC17 pad 5: /motor_driver8/M0_4 -> /motor_driver16/M0_4
- IC17 pad 6: /motor_driver8/M1_1 -> /motor_driver16/M1_1
- IC17 pad 9: /motor_driver8/DATA_OUT -> /motor_driver16/DATA_OUT
- IC19 pad 10: SHIFT_CLOCK -> LATCH_CLOCK
- IC19 pad 11: /motor_driver9/M1_23 -> /motor_driver18/M1_23
- IC19 pad 12: /motor_driver9/M1_4 -> /motor_driver18/M1_4
- IC19 pad 13: /motor_driver9/VCC_HALL -> /motor_driver18/VCC_HALL
- IC19 pad 15: LATCH_CLOCK -> SHIFT_CLOCK
- IC19 pad 2: /motor_driver8/DATA_OUT -> /motor_driver17/DATA_OUT
- IC19 pad 3: /motor_driver9/M0_1 -> /motor_driver18/M0_1
- IC19 pad 4: /motor_driver9/M0_23 -> /motor_driver18/M0_23
- IC19 pad 5: /motor_driver9/M0_4 -> /motor_driver18/M0_4
- IC19 pad 6: /motor_driver9/M1_1 -> /motor_driver18/M1_1
- IC19 pad 9: /motor_driver10/DATA_IN -> /motor_driver18/DATA_OUT
- IC21 pad 10: SHIFT_CLOCK -> LATCH_CLOCK
- IC21 pad 11: /motor_driver10/M1_23 -> /motor_driver20/M1_23
- IC21 pad 12: /motor_driver10/M1_4 -> /motor_driver20/M1_4
- IC21 pad 13: /motor_driver10/VCC_HALL -> /motor_driver20/VCC_HALL
- IC21 pad 15: LATCH_CLOCK -> SHIFT_CLOCK
- IC21 pad 2: /motor_driver10/DATA_IN -> /motor_driver19/DATA_OUT
- IC21 pad 3: /motor_driver10/M0_1 -> /motor_driver20/M0_1
- IC21 pad 4: /motor_driver10/M0_23 -> /motor_driver20/M0_23
- IC21 pad 5: /motor_driver10/M0_4 -> /motor_driver20/M0_4
- IC21 pad 6: /motor_driver10/M1_1 -> /motor_driver20/M1_1
- IC21 pad 9: /motor_driver10/DATA_OUT -> /motor_driver20/DATA_OUT
- IC23 pad 10: SHIFT_CLOCK -> LATCH_CLOCK
- IC23 pad 11: /motor_driver11/M1_23 -> /motor_driver22/M1_23
- IC23 pad 12: /motor_driver11/M1_4 -> /motor_driver22/M1_4
- IC23 pad 13: /motor_driver11/VCC_HALL -> /motor_driver22/VCC_HALL
- IC23 pad 15: LATCH_CLOCK -> SHIFT_CLOCK
- IC23 pad 2: /motor_driver10/DATA_OUT -> /motor_driver21/DATA_OUT
- IC23 pad 3: /motor_driver11/M0_1 -> /motor_driver22/M0_1
- IC23 pad 4: /motor_driver11/M0_23 -> /motor_driver22/M0_23
- IC23 pad 5: /motor_driver11/M0_4 -> /motor_driver22/M0_4
- IC23 pad 6: /motor_driver11/M1_1 -> /motor_driver22/M1_1
- IC23 pad 9: /motor_driver11/DATA_OUT -> /motor_driver22/DATA_OUT
- IC3 pad 10: SHIFT_CLOCK -> LATCH_CLOCK
- IC3 pad 11: /motor_driver1/M1_23 -> /motor_driver2/M1_23
- IC3 pad 12: /motor_driver1/M1_4 -> /motor_driver2/M1_4
- IC3 pad 13: /motor_driver1/VCC_HALL -> /motor_driver2/VCC_HALL
- IC3 pad 15: LATCH_CLOCK -> SHIFT_CLOCK
- IC3 pad 2: /motor_driver0/DATA_OUT -> /motor_driver1/DATA_OUT
- IC3 pad 3: /motor_driver1/M0_1 -> /motor_driver2/M0_1
- IC3 pad 4: /motor_driver1/M0_23 -> /motor_driver2/M0_23
- IC3 pad 5: /motor_driver1/M0_4 -> /motor_driver2/M0_4
- IC3 pad 6: /motor_driver1/M1_1 -> /motor_driver2/M1_1
- IC3 pad 9: /motor_driver1/DATA_OUT -> /motor_driver2/DATA_OUT
- IC5 pad 10: SHIFT_CLOCK -> LATCH_CLOCK
- IC5 pad 11: /motor_driver2/M1_23 -> /motor_driver4/M1_23
- IC5 pad 12: /motor_driver2/M1_4 -> /motor_driver4/M1_4
- IC5 pad 13: /motor_driver2/VCC_HALL -> /motor_driver4/VCC_HALL
- IC5 pad 15: LATCH_CLOCK -> SHIFT_CLOCK
- IC5 pad 2: /motor_driver1/DATA_OUT -> /motor_driver3/DATA_OUT
- IC5 pad 3: /motor_driver2/M0_1 -> /motor_driver4/M0_1
- IC5 pad 4: /motor_driver2/M0_23 -> /motor_driver4/M0_23
- IC5 pad 5: /motor_driver2/M0_4 -> /motor_driver4/M0_4
- IC5 pad 6: /motor_driver2/M1_1 -> /motor_driver4/M1_1
- IC5 pad 9: /motor_driver2/DATA_OUT -> /motor_driver4/DATA_OUT
- IC7 pad 10: SHIFT_CLOCK -> LATCH_CLOCK
- IC7 pad 11: /motor_driver3/M1_23 -> /motor_driver6/M1_23
- IC7 pad 12: /motor_driver3/M1_4 -> /motor_driver6/M1_4
- IC7 pad 13: /motor_driver3/VCC_HALL -> /motor_driver6/VCC_HALL
- IC7 pad 15: LATCH_CLOCK -> SHIFT_CLOCK
- IC7 pad 2: /motor_driver2/DATA_OUT -> /motor_driver5/DATA_OUT
- IC7 pad 3: /motor_driver3/M0_1 -> /motor_driver6/M0_1
- IC7 pad 4: /motor_driver3/M0_23 -> /motor_driver6/M0_23
- IC7 pad 5: /motor_driver3/M0_4 -> /motor_driver6/M0_4
- IC7 pad 6: /motor_driver3/M1_1 -> /motor_driver6/M1_1
- IC7 pad 9: /motor_driver3/DATA_OUT -> /motor_driver6/DATA_OUT
- IC9 pad 10: SHIFT_CLOCK -> LATCH_CLOCK
- IC9 pad 11: /motor_driver4/M1_23 -> /motor_driver8/M1_23
- IC9 pad 12: /motor_driver4/M1_4 -> /motor_driver8/M1_4
- IC9 pad 13: /motor_driver4/VCC_HALL -> /motor_driver8/VCC_HALL
- IC9 pad 15: LATCH_CLOCK -> SHIFT_CLOCK
- IC9 pad 2: /motor_driver3/DATA_OUT -> /motor_driver7/DATA_OUT
- IC9 pad 3: /motor_driver4/M0_1 -> /motor_driver8/M0_1
- IC9 pad 4: /motor_driver4/M0_23 -> /motor_driver8/M0_23
- IC9 pad 5: /motor_driver4/M0_4 -> /motor_driver8/M0_4
- IC9 pad 6: /motor_driver4/M1_1 -> /motor_driver8/M1_1
- IC9 pad 9: /motor_driver4/DATA_OUT -> /motor_driver8/DATA_OUT
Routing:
- net VCC: track 0.00 -> 720.5 mm, vias 0 -> 46
- net SHIFT_CLOCK: track 0.00 -> 572.2 mm, vias 0 -> 24
- net LATCH_CLOCK: track 0.00 -> 500.2 mm, vias 0 -> 24
- net HALL_IN: track 0.00 -> 439.7 mm
- net /control_board/DATA_OUT: track 0.00 -> 59.4 mm
- net /motor_driver10/DATA_IN: track 0.00 -> 58.9 mm, vias 0 -> 4
- net /motor_driver8/DATA_OUT: track 0.00 -> 55.4 mm
- net /motor_driver5/DATA_OUT: track 0.00 -> 54.8 mm
- net /motor_driver2/DATA_OUT: track 0.00 -> 47.4 mm, vias 0 -> 2
- net /motor_driver4/DATA_OUT: track 0.00 -> 31.5 mm, vias 0 -> 2
- net /motor_driver3/DATA_OUT: track 0.00 -> 31.1 mm, vias 0 -> 2
- net /motor_driver8/M1_23: track 0.00 -> 27.8 mm
- net /motor_driver6/M1_23: track 0.00 -> 27.8 mm
- net /motor_driver7/M1_23: track 0.00 -> 27.8 mm
- net /motor_driver3/M1_23: track 0.00 -> 27.8 mm
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- added copper zone on F.Cu, net GND
- added copper zone on B.Cu, net VCC
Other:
- board outline added: 263.5 x 52 mm
